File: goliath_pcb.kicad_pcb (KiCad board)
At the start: 2 copper layers, 140 x 90 mm, 100 parts, among them J1 RJ45_LED, J10 Conn_01x04_Male, J11 Screw_Terminal_01x02, J12 Screw_Terminal_01x02, J13 Screw_Terminal_01x02, J14 Conn_01x02_Male, J15 Conn_01x02_Male, J2 RJ45_LED, J3 RJ45_LED, J4 RJ45_LED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

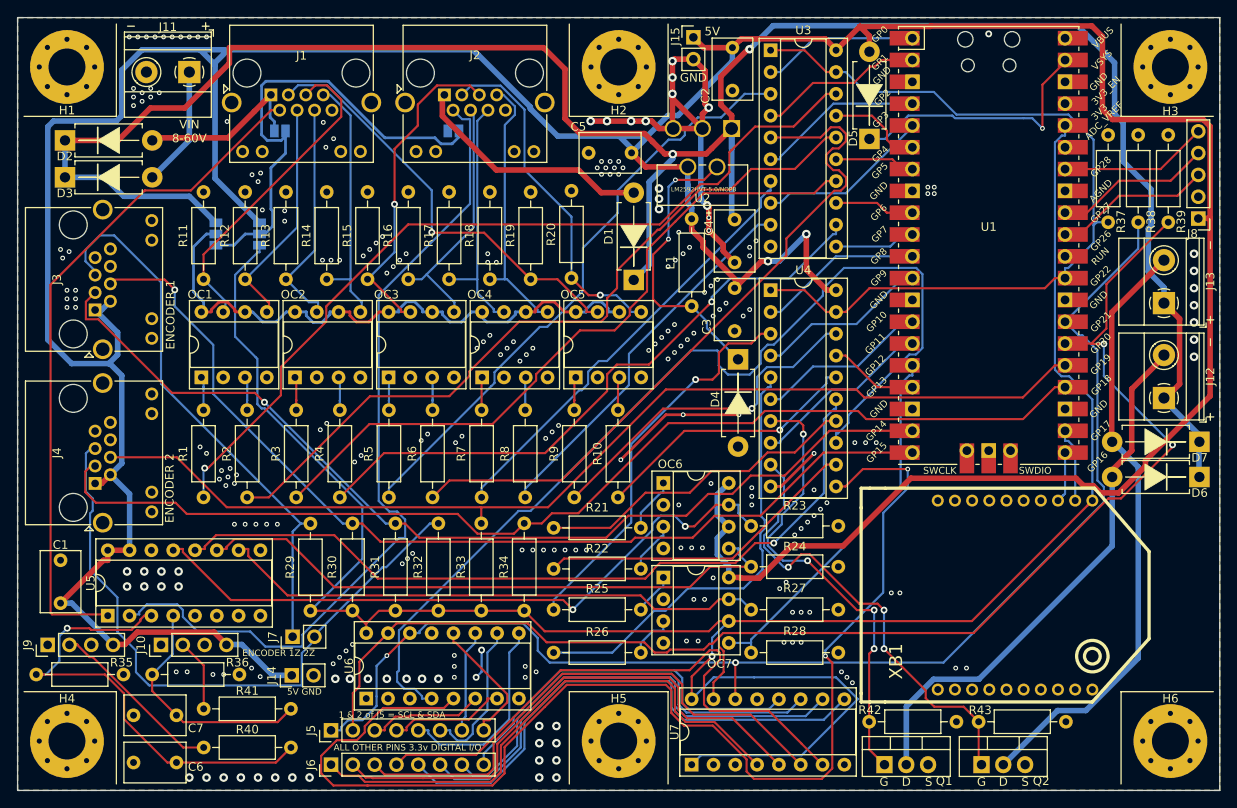
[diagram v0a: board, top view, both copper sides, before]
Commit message: Adjust via stitching to alighn with silkscreen text
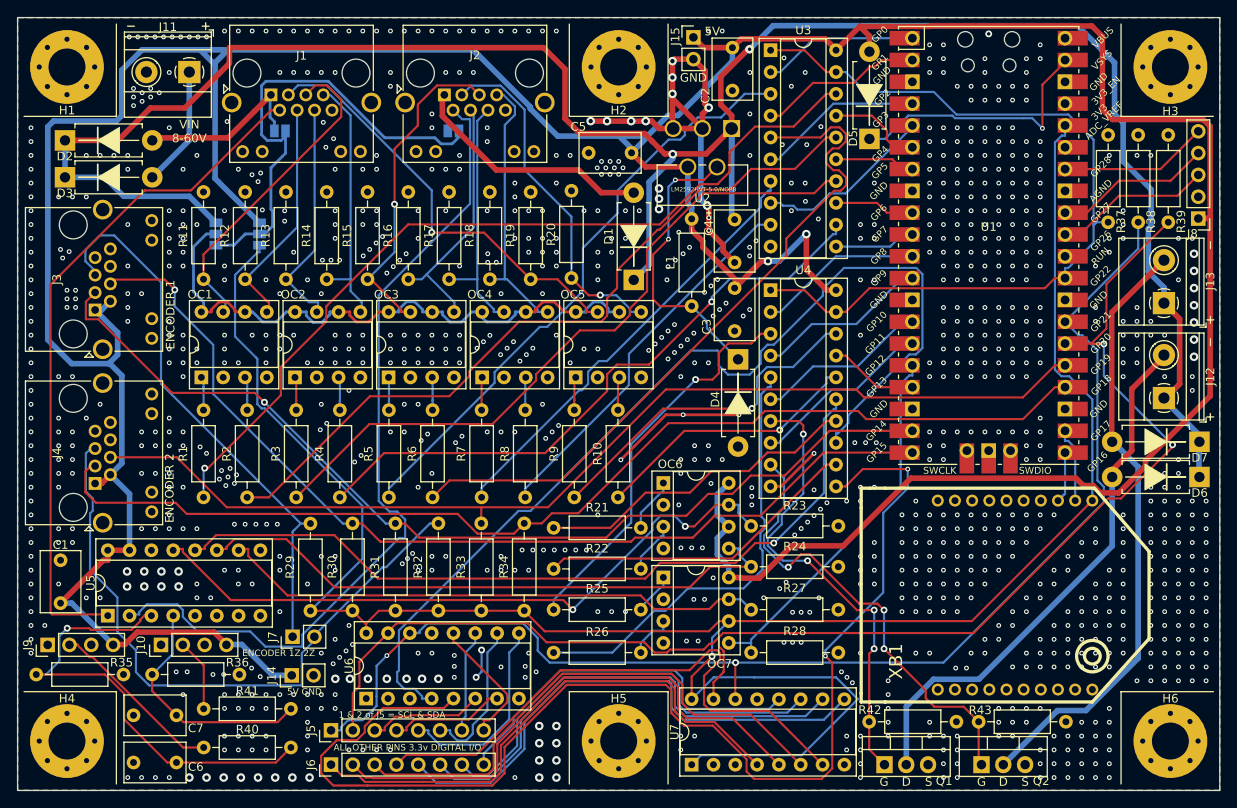
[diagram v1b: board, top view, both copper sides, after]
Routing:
- net Net-(U1-Pad5): track 20.3 -> 21.0 mm
- net GND: vias 248 -> 1133
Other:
- board text added: "Designed by Amelia Deck for ILLINOIS TECH ROBOTICS Robot Interfacing Board (RIB) V1.0-RC1 inspired by GOLIATH design by Nash Kaminski with help from Scarlett Kadan Iliyan Jivraj"
- board text added: "{ "ViaStitching": "0.1", "stitch_zone_0": { "HSpacing": "2", "VSpacing": "2", "Clearance": "0.2", "Randomize": false }, "stitch_zone_1": { "HSpacing": "2", "VSpacing": "2", "Clearance": "0", "Randomize": false } }"
- board text removed: "Designed by Amelia Deck for ILLINOIS TECH ROBOTICS Robot Interfacing Board (RIB) V1.0-RC1"
- board text removed: "inspired by GOLIATH design by Nash Kaminski"
- board text removed: "with help from Scarlett Kadan Iliyan Jivraj"

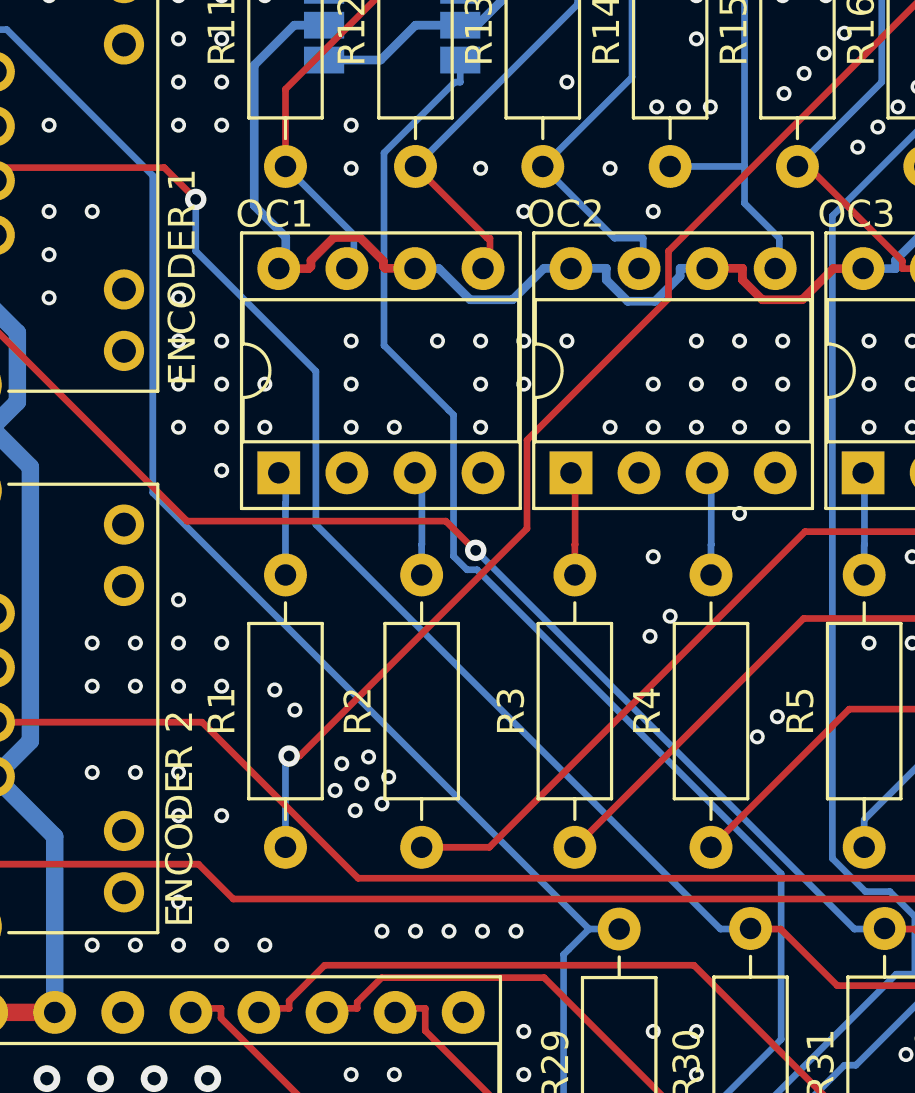
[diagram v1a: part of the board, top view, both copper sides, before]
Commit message: Fix other silkscreen text
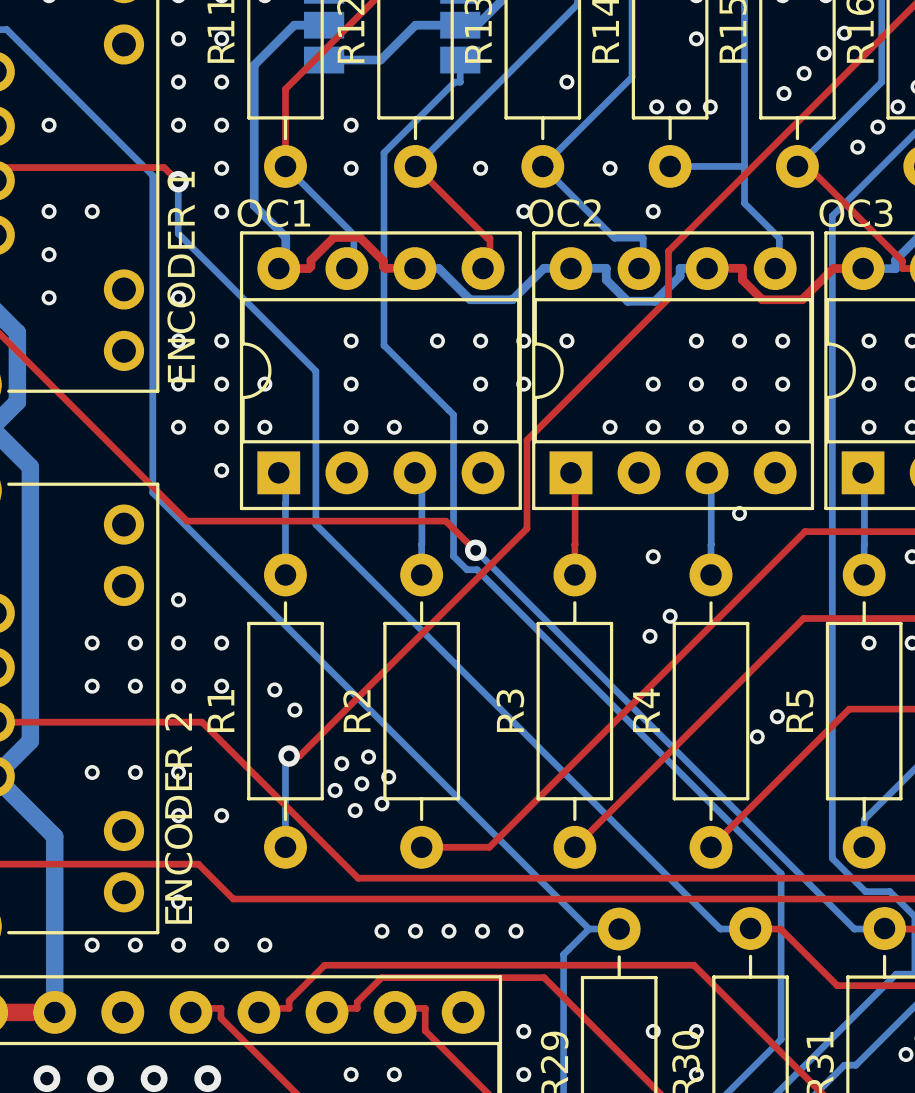
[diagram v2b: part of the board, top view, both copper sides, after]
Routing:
- net GND: vias 1133 -> 1135
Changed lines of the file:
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@@
   )
   (gr_line (start 170.8 61.7) (end 171.8 60.925) (layer "B.SilkS") (width 0.15))
-  (gr_line (start 56.05 70.295) (end 57.32 70.295) (layer "B.SilkS") (width 0.15))
-  (gr_line (start 56.05 74.25) (end 57.32 74.25) (layer "B.SilkS") (width 0.15))
+  (gr_line (start 56.25 70.295) (end 57.32 70.295) (layer "B.SilkS") (width 0.15))
+  (gr_line (start 56.35 74.25) (end 57.32 74.25) (layer "B.SilkS") (width 0.15))
   (gr_line (start 170.05 69.2) (end 171.8 70) (layer "B.SilkS") (width 0.15))
   (gr_line (start 67.48 74.105) (end 64.94 74.105) (layer "B.SilkS") (width 0.15))
@@
     (effects (font (size 0.75 0.75) (thickness 0.15)) (justify mirror))
   )
-  (gr_text "Logic Voltage Output\nVIN/OSMC  5/3v3   " (at 54.145 72 90) (layer "B.SilkS")
+  (gr_text "Logic Voltage Output\nVIN/OSMC  5/3v3   " (at 54.75 72 90) (layer "B.SilkS")
     (effects (font (size 1 1) (thickness 0.15)) (justify mirror))
   )
@@
   (via (at 91.8 48.56) (size 0.56) (drill 0.3) (layers "F.Cu" "B.Cu") (free) (net 1))
   (via (at 106 64.5) (size 0.56) (drill 0.3) (layers "F.Cu" "B.Cu") (free) (net 1))
+  (via (at 54.77 77.54) (size 0.56) (drill 0.3) (layers "F.Cu" "B.Cu") (free) (net 1))
   (via (at 114.75 119.6) (size 0.56) (drill 0.3) (layers "F.Cu" "B.Cu") (net 1))
   (via (at 172.3 90.42) (size 0.56) (drill 0.3) (layers "F.Cu" "B.Cu") (free) (net 1))
@@
   (via (at 75.7 69.49) (size 0.56) (drill 0.3) (layers "F.Cu" "B.Cu") (free) (net 1))
   (via (at 151.37 64.66) (size 0.56) (drill 0.3) (layers "F.Cu" "B.Cu") (free) (net 1))
+  (via (at 54.77 79.15) (size 0.56) (drill 0.3) (layers "F.Cu" "B.Cu") (free) (net 1))
   (via (at 117.56 48.56) (size 0.56) (drill 0.3) (layers "F.Cu" "B.Cu") (free) (net 1))
   (via (at 148.15 53.39) (size 0.56) (drill 0.3) (layers "F.Cu" "B.Cu") (free) (net 1))
@@
   (segment (start 77.7361 108.031) (end 106.939 108.031) (width 0.25) (layer "F.Cu") (net 81))
   (segment (start 116.677 105.01) (end 122.015 105.01) (width 0.25) (layer "F.Cu") (net 81))
-  (segment (start 52.6244 77.512) (end 46.305 77.512) (width 0.25) (layer "F.Cu") (net 81))
   (segment (start 75.6251 105.92) (end 77.7361 108.031) (width 0.25) (layer "F.Cu") (net 81))
   (segment (start 74.5 105.92) (end 75.6251 105.92) (width 0.25) (layer "F.Cu") (net 81))
@@
   (segment (start 106.939 108.031) (end 107.405 107.564) (width 0.25) (layer "F.Cu") (net 81))
   (segment (start 114.122 107.564) (end 116.677 105.01) (width 0.25) (layer "F.Cu") (net 81))
-  (segment (start 53.8011 78.6989) (end 53.8011 78.6887) (width 0.25) (layer "F.Cu") (net 81))
+  (segment (start 52.6244 77.512) (end 46.305 77.512) (width 0.25) (layer "F.Cu") (net 81))
+  (segment (start 53.15 78.0376) (end 52.6244 77.512) (width 0.25) (layer "F.Cu") (net 81))
   (segment (start 129.365 97.6597) (end 139.7 97.6597) (width 0.25) (layer "F.Cu") (net 81))
-  (segment (start 53.8011 78.6887) (end 52.6244 77.512) (width 0.25) (layer "F.Cu") (net 81))
-  (via (at 53.8011 78.6989) (size 0.8) (drill 0.4) (layers "F.Cu" "B.Cu") (net 81))
-  (segment (start 73.3749 105.92) (end 58.2852 90.8303) (width 0.25) (layer "B.Cu") (net 81))
-  (segment (start 53.8011 80.6271) (end 53.8011 78.6989) (width 0.25) (layer "B.Cu") (net 81))
-  (segment (start 58.2852 85.1112) (end 53.8011 80.6271) (width 0.25) (layer "B.Cu") (net 81))
-  (segment (start 58.2852 90.8303) (end 58.2852 85.1112) (width 0.25) (layer "B.Cu") (net 81))
-  (segment (start 74.5 105.92) (end 73.3749 105.92) (width 0.25) (layer "B.Cu") (net 81))
+  (via (at 53.15 78.0376) (size 0.8) (drill 0.4) (layers "F.Cu" "B.Cu") (net 81))
+  (segment (start 58.2852 85.1112) (end 58.2852 90.8303) (width 0.25) (layer "B.Cu") (net 81))
+  (segment (start 53.15 78.0376) (end 53.15 79.976) (width 0.25) (layer "B.Cu") (net 81))
+  (segment (start 73.3749 105.92) (end 74.5 105.92) (width 0.25) (layer "B.Cu") (net 81))
+  (segment (start 53.15 79.976) (end 58.2852 85.1112) (width 0.25) (layer "B.Cu") (net 81))
+  (segment (start 58.2852 90.8303) (end 73.3749 105.92) (width 0.25) (layer "B.Cu") (net 81))
   (segment (start 86.744365 104.8) (end 55.202708 104.8) (width 0.25) (layer "F.Cu") (net 82))
   (segment (start 122.518 92.8136) (end 121.105 94.2261) (width 0.25) (layer "F.Cu") (net 82))
@@
       4e08259c-72a2-4109-b178-3d9820d00dd7
       4e60b395-1014-419a-b449-3757948a0b73
+      4e8f1c8b-4090-4f57-bc21-576b47bac4a0
       4f3586a2-5239-494b-ba34-23f0fc9bd2ed
       4f9182c5-9042-4c4e-8816-87f23f017bd3
@@
       72f9fb7b-cfca-4605-8aff-8797debfd44b
       73023c24-0f8e-40d8-9185-18ebce72639c
+      736ac4af-a4b0-4d82-ade9-32c50c539acf
       73a3dc5e-8ca9-494f-b9a8-7924c30b37cc
       73c74605-2d3d-41e4-9b5b-27b26ca0e817

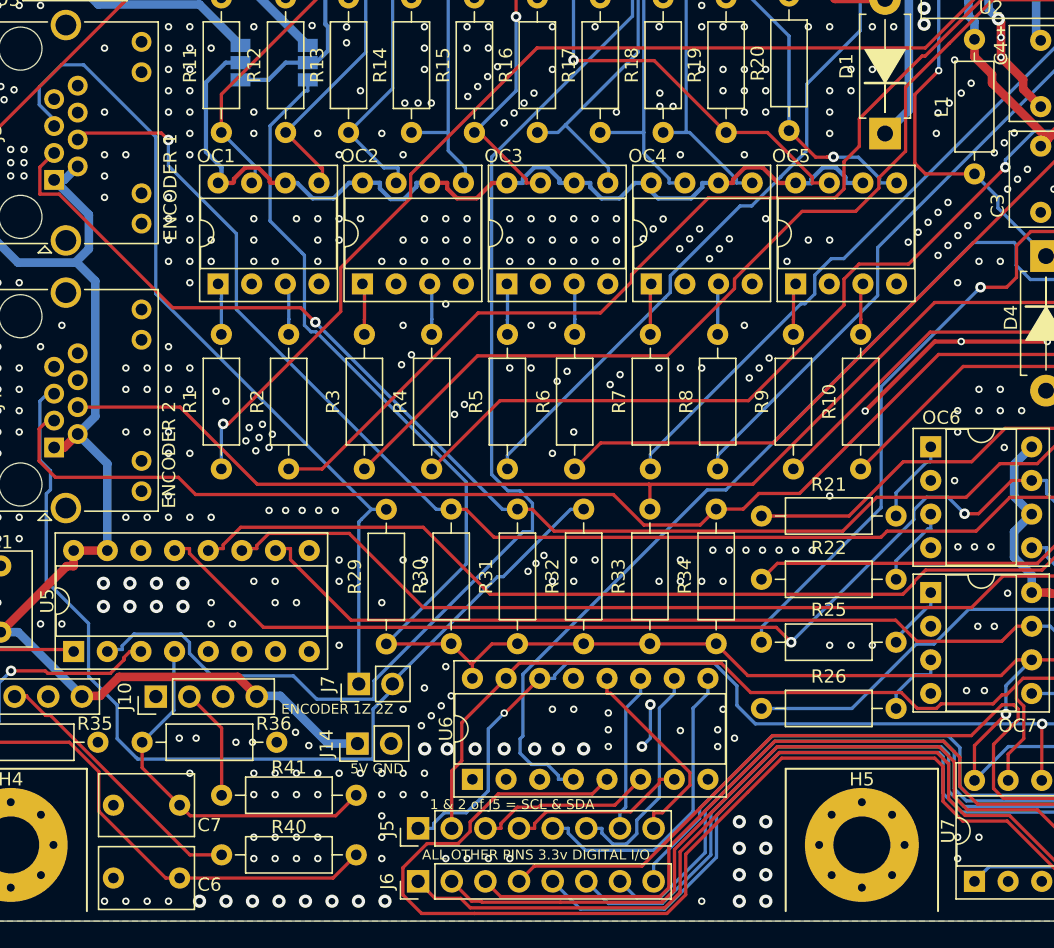
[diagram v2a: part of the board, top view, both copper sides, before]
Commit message: Remove extra vias
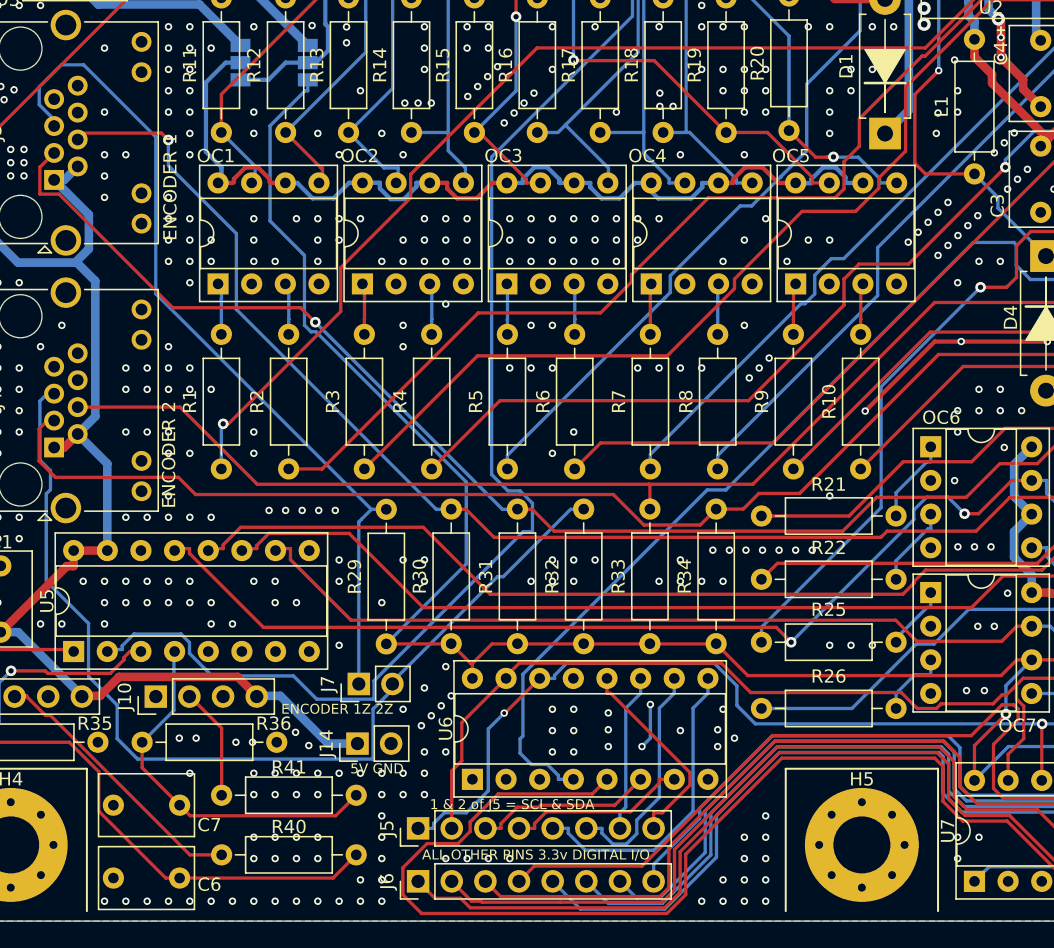
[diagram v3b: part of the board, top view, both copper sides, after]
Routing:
- net GND: vias 1135 -> 1128

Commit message: More via work
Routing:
- net GND: vias 1128 -> 1116
